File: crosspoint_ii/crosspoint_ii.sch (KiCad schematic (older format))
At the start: 1 part, among them P1 DIN_41612_128P

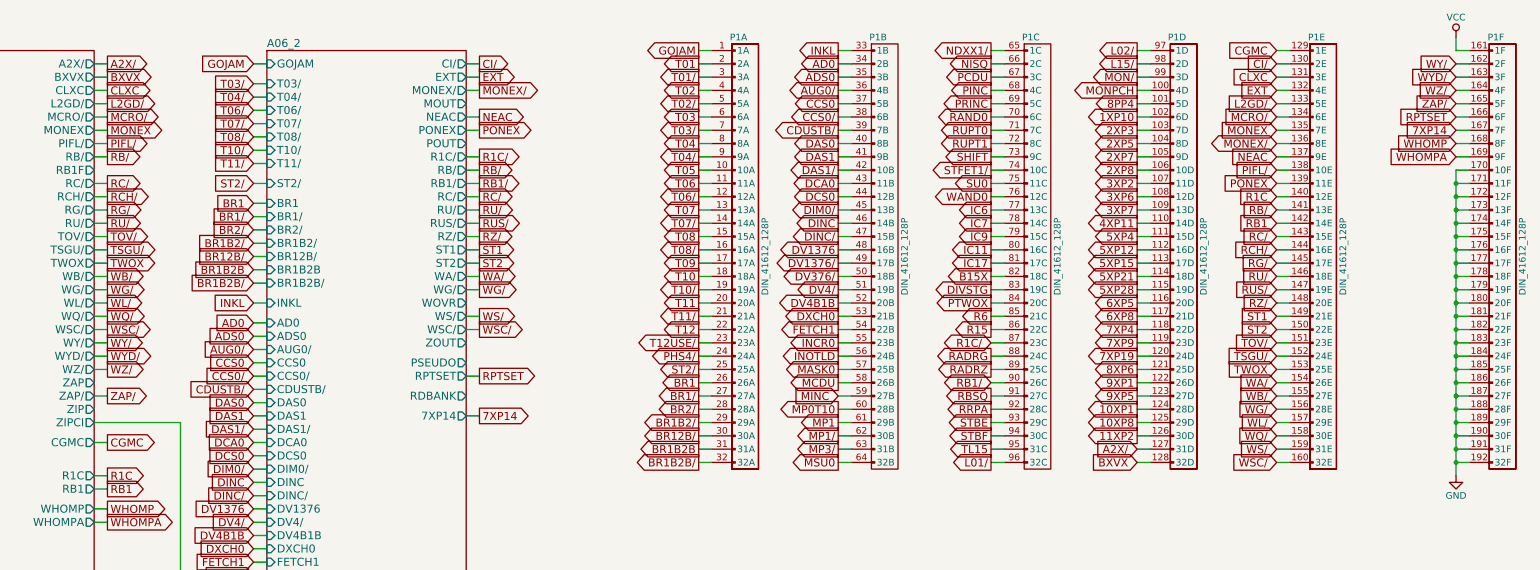
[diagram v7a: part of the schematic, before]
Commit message: Added and tied in module 15, the rupt service (and banking/rope+strand selection)
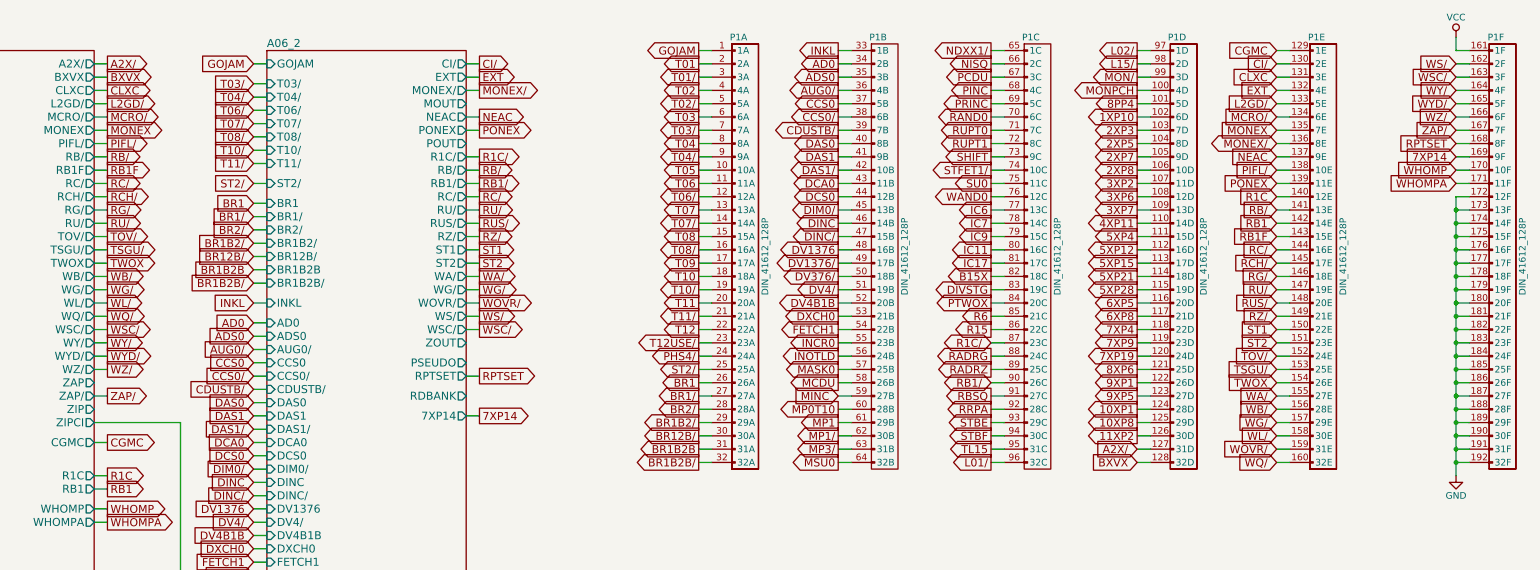
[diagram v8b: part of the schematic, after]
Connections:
- net 7XP14: now also P1.169 (9F); no longer P1.167 (7F)
- net GND: no longer P1.170 (10F), P1.171 (11F)
- net RC/: now also P1.144 (16E); no longer P1.143 (15E)
- net RCH/: now also P1.145 (17E); no longer P1.144 (16E)
- net RG/: now also P1.146 (18E); no longer P1.145 (17E)
- net RPTSET: now also P1.168 (8F); no longer P1.166 (6F)
- net RU/: now also P1.147 (19E); no longer P1.146 (18E)
- net RUS/: now also P1.148 (20E); no longer P1.147 (19E)
- net RZ/: now also P1.149 (21E); no longer P1.148 (20E)
- net ST1: now also P1.150 (22E); no longer P1.149 (21E)
- net ST2: now also P1.151 (23E); no longer P1.150 (22E)
- net TOV/: now also P1.152 (24E); no longer P1.151 (23E)
- net TSGU/: now also P1.153 (25E); no longer P1.152 (24E)
- net TWOX: now also P1.154 (26E); no longer P1.153 (25E)
- net WA/: now also P1.155 (27E); no longer P1.154 (26E)
- net WB/: now also P1.156 (28E); no longer P1.155 (27E)
- net WG/: now also P1.157 (29E); no longer P1.156 (28E)
- net WHOMP: now also P1.170 (10F); no longer P1.168 (8F)
- net WHOMPA: now also P1.171 (11F); no longer P1.169 (9F)
- net WL/: now also P1.158 (30E); no longer P1.157 (29E)
- net WQ/: now also P1.160 (32E); no longer P1.158 (30E)
- net WS/: now also P1.162 (2F); no longer P1.159 (31E)
- net WSC/: now also P1.163 (3F); no longer P1.160 (32E)
- net WY/: now also P1.164 (4F); no longer P1.162 (2F)
- net WYD/: now also P1.165 (5F); no longer P1.163 (3F)
- net WZ/: now also P1.166 (6F); no longer P1.164 (4F)
- net ZAP/: now also P1.167 (7F); no longer P1.165 (5F)
- new net RB1F: P1.143 (15E)
- new net WOVR/: P1.159 (31E)
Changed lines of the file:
@@
 F46 "MON/" I L 6600 9750 60
 F47 "FETCH1" I L 6600 6300 60
-F48 "WOVR" O R 8100 4350 60
+F48 "WOVR/" O R 8100 4350 60
 F49 "WSC/" O R 8100 4550 60
 F50 "WG/" O R 8100 4250 60
@@
 Wire Wire Line
 	8200 4050 8100 4050
-Text GLabel 14200 4450 0    60   Input ~ 0
+Text GLabel 14200 4550 0    60   Input ~ 0
 ST1
 Wire Wire Line
-	14200 4450 14300 4450
-Text GLabel 14200 4550 0    60   Input ~ 0
+	14200 4550 14300 4550
+Text GLabel 14200 4650 0    60   Input ~ 0
 ST2
 Wire Wire Line
-	14200 4550 14300 4550
+	14200 4650 14300 4650
 Text GLabel 5400 3950 2    60   Output ~ 0
 TSGU/
 Wire Wire Line
 	5400 3950 5300 3950
-Text GLabel 14200 4750 0    60   Input ~ 0
+Text GLabel 14200 4850 0    60   Input ~ 0
 TSGU/
 Wire Wire Line
-	14200 4750 14300 4750
+	14200 4850 14300 4850
 Text GLabel 3650 7000 0    60   Input ~ 0
 3XP7
@@
 Wire Wire Line
 	8200 5200 8100 5200
-Text GLabel 15550 3050 0    60   Input ~ 0
+Text GLabel 15550 3250 0    60   Input ~ 0
 7XP14
 Wire Wire Line
-	15550 3050 15650 3050
+	15550 3250 15650 3250
 Text GLabel 8200 4900 2    60   Output ~ 0
 RPTSET
 Wire Wire Line
 	8200 4900 8100 4900
-Text GLabel 15550 2950 0    60   Input ~ 0
+Text GLabel 15550 3150 0    60   Input ~ 0
 RPTSET
 Wire Wire Line
-	15550 2950 15650 2950
+	15550 3150 15650 3150
 Text GLabel 5400 3850 2    60   Output ~ 0
 TOV/
 Wire Wire Line
 	5400 3850 5300 3850
-Text GLabel 14200 4650 0    60   Input ~ 0
+Text GLabel 14200 4750 0    60   Input ~ 0
 TOV/
 Wire Wire Line
-	14200 4650 14300 4650
+	14200 4750 14300 4750
 Text GLabel 5400 2550 2    60   Output ~ 0
 A2X/
@@
 Wire Wire Line
 	5400 3550 5300 3550
-Text GLabel 14200 3950 0    60   Input ~ 0
+Text GLabel 14200 4050 0    60   Input ~ 0
 RCH/
 Wire Wire Line
-	14200 3950 14300 3950
+	14200 4050 14300 4050
 Text GLabel 5400 3450 2    60   Output ~ 0
 RC/
@@
 Wire Wire Line
 	8200 3550 8100 3550
-Text GLabel 14200 3850 0    60   Input ~ 0
+Text GLabel 14200 3950 0    60   Input ~ 0
 RC/
 Wire Wire Line
-	14200 3850 14300 3850
+	14200 3950 14300 3950
 Text GLabel 5400 3650 2    60   Output ~ 0
 RG/
 Wire Wire Line
 	5400 3650 5300 3650
-Text GLabel 14200 4050 0    60   Input ~ 0
+Text GLabel 14200 4150 0    60   Input ~ 0
 RG/
 Wire Wire Line
-	14200 4050 14300 4050
+	14200 4150 14300 4150
 $Comp
 L DIN_41612_128P P1
@@
 Connection ~ 15550 3750
 Wire Wire Line
-	15550 3450 15650 3450
-Wire Wire Line
-	15550 3350 15650 3350
-Connection ~ 15550 3450
-Wire Wire Line
 	15550 3650 15650 3650
 Wire Wire Line
 	15550 3550 15650 3550
 Connection ~ 15550 3650
-Connection ~ 15550 3550
 Text GLabel 8200 3750 2    60   Output ~ 0
 RUS/
 Wire Wire Line
 	8200 3750 8100 3750
-Text GLabel 14200 4150 0    60   Input ~ 0
+Text GLabel 14200 4250 0    60   Input ~ 0
 RU/
 Wire Wire Line
-	14200 4150 14300 4150
+	14200 4250 14300 4250
 Text GLabel 5400 3750 2    60   Output ~ 0
 RU/
@@
 Wire Wire Line
 	8200 3650 8100 3650
-Text GLabel 14200 4250 0    60   Input ~ 0
+Text GLabel 14200 4350 0    60   Input ~ 0
 RUS/
 Wire Wire Line
-	14200 4250 14300 4250
+	14200 4350 14300 4350
 Text GLabel 8200 3850 2    60   Output ~ 0
 RZ/
 Wire Wire Line
 	8200 3850 8100 3850
-Text GLabel 14200 4350 0    60   Input ~ 0
+Text GLabel 14200 4450 0    60   Input ~ 0
 RZ/
 Wire Wire Line
-	14200 4350 14300 4350
+	14200 4450 14300 4450
 Text GLabel 8200 4150 2    60   Output ~ 0
 WA/
 Wire Wire Line
 	8200 4150 8100 4150
-Text GLabel 14200 4950 0    60   Input ~ 0
+Text GLabel 14200 5050 0    60   Input ~ 0
 WA/
 Wire Wire Line
-	14200 4950 14300 4950
+	14200 5050 14300 5050
 Text GLabel 5400 4150 2    60   Output ~ 0
 WB/
 Wire Wire Line
 	5400 4150 5300 4150
-Text GLabel 14200 5050 0    60   Input ~ 0
+Text GLabel 14200 5150 0    60   Input ~ 0
 WB/
 Wire Wire Line
-	14200 5050 14300 5050
+	14200 5150 14300 5150
 Text GLabel 5400 4250 2    60   Output ~ 0
 WG/
@@
 Wire Wire Line
 	8200 4250 8100 4250
-Text GLabel 14200 5150 0    60   Input ~ 0
+Text GLabel 14200 5250 0    60   Input ~ 0
 WG/
 Wire Wire Line
-	14200 5150 14300 5150
+	14200 5250 14300 5250
 Text GLabel 5400 4350 2    60   Output ~ 0
 WL/
 Wire Wire Line
 	5400 4350 5300 4350
-Text GLabel 14200 5250 0    60   Input ~ 0
+Text GLabel 14200 5350 0    60   Input ~ 0
 WL/
 Wire Wire Line
-	14200 5250 14300 5250
+	14200 5350 14300 5350
 Text GLabel 5400 4450 2    60   Output ~ 0
 WQ/
 Wire Wire Line
 	5400 4450 5300 4450
-Text GLabel 14200 5350 0    60   Input ~ 0
+Text GLabel 14200 5550 0    60   Input ~ 0
 WQ/
 Wire Wire Line
-	14200 5350 14300 5350
+	14200 5550 14300 5550
 Text GLabel 5400 4550 2    60   Output ~ 0
 WSC/
@@
 Wire Wire Line
 	8200 4550 8100 4550
-Text GLabel 14200 5550 0    60   Input ~ 0
+Text GLabel 15550 2650 0    60   Input ~ 0
 WSC/
 Wire Wire Line
-	14200 5550 14300 5550
+	15550 2650 15650 2650
 Text GLabel 8200 4450 2    60   Output ~ 0
 WS/
 Wire Wire Line
 	8200 4450 8100 4450
-Text GLabel 14200 5450 0    60   Input ~ 0
+Text GLabel 15550 2550 0    60   Input ~ 0
 WS/
 Wire Wire Line
-	14200 5450 14300 5450
+	15550 2550 15650 2550
 Text GLabel 5400 4750 2    60   Output ~ 0
 WYD/
 Wire Wire Line
 	5400 4750 5300 4750
-Text GLabel 15550 2650 0    60   Input ~ 0
+Text GLabel 15550 2850 0    60   Input ~ 0
 WYD/
 Wire Wire Line
-	15550 2650 15650 2650
+	15550 2850 15650 2850
 Text GLabel 5400 4650 2    60   Output ~ 0
 WY/
 Wire Wire Line
 	5400 4650 5300 4650
-Text GLabel 15550 2550 0    60   Input ~ 0
+Text GLabel 15550 2750 0    60   Input ~ 0
 WY/
 Wire Wire Line
-	15550 2550 15650 2550
+	15550 2750 15650 2750
 Text GLabel 5400 4850 2    60   Output ~ 0
 WZ/
 Wire Wire Line
 	5400 4850 5300 4850
-Text GLabel 15550 2750 0    60   Input ~ 0
+Text GLabel 15550 2950 0    60   Input ~ 0
 WZ/
 Wire Wire Line
-	15550 2750 15650 2750
+	15550 2950 15650 2950
 Text GLabel 5400 5050 2    60   Output ~ 0
 ZAP/
 Wire Wire Line
 	5400 5050 5300 5050
-Text GLabel 15550 2850 0    60   Input ~ 0
+Text GLabel 15550 3050 0    60   Input ~ 0
 ZAP/
 Wire Wire Line
-	15550 2850 15650 2850
+	15550 3050 15650 3050
 Text GLabel 5400 2750 2    60   Output ~ 0
 CLXC
@@
 Wire Wire Line
 	5400 4050 5300 4050
-Text GLabel 14200 4850 0    60   Input ~ 0
+Text GLabel 14200 4950 0    60   Input ~ 0
 TWOX
 Wire Wire Line
-	14200 4850 14300 4850
+	14200 4950 14300 4950
 Text GLabel 5400 3050 2    60   Output ~ 0
 MONEX
@@
 Wire Wire Line
 	3650 8500 3750 8500
-Wire Wire Line
-	15550 3350 15550 5650
 Text GLabel 12050 2550 0    60   Output ~ 0
 NISQ
@@
 Wire Wire Line
 	5400 6000 5300 6000
-Text GLabel 15550 3250 0    60   Input ~ 0
+Text GLabel 15550 3450 0    60   Input ~ 0
 WHOMPA
 Wire Wire Line
-	15550 3250 15650 3250
-Text GLabel 15550 3150 0    60   Input ~ 0
+	15550 3450 15650 3450
+Text GLabel 15550 3350 0    60   Input ~ 0
 WHOMP
 Wire Wire Line
-	15550 3150 15650 3150
+	15550 3350 15650 3350
+Text GLabel 5400 3350 2    60   Output ~ 0
+RB1F
+Wire Wire Line
+	5400 3350 5300 3350
+Wire Wire Line
+	15550 3550 15550 5650
+Text GLabel 14200 3850 0    60   Input ~ 0
+RB1F
+Wire Wire Line
+	14200 3850 14300 3850
+Text GLabel 8200 4350 2    60   Output ~ 0
+WOVR/
+Wire Wire Line
+	8200 4350 8100 4350
+Text GLabel 14200 5450 0    60   Input ~ 0
+WOVR/
+Wire Wire Line
+	14200 5450 14300 5450
 $EndSCHEMATC
